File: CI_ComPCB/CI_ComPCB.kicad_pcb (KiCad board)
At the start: 2 copper layers, 83 x 85 mm, 37 parts, among them J1001 Conn_01x02_Male, J1002 Conn_01x02_Male, J1003 Conn_01x15_Female, J1004 Conn_01x15_Female, J1005 Conn_01x06_Female, J1006 Conn_01x06_Female, J1008 Conn_01x02_Male, J1009 RJ45_LED_Shielded, J1010 RJ45_LED_Shielded, J1011 Conn_01x01_Female, J1012 Conn_01x01_Female, J1013 Conn_02x04_Odd_Even, Q1001 IRF9540N, U1001 ESP32s, U1002 TPS54331

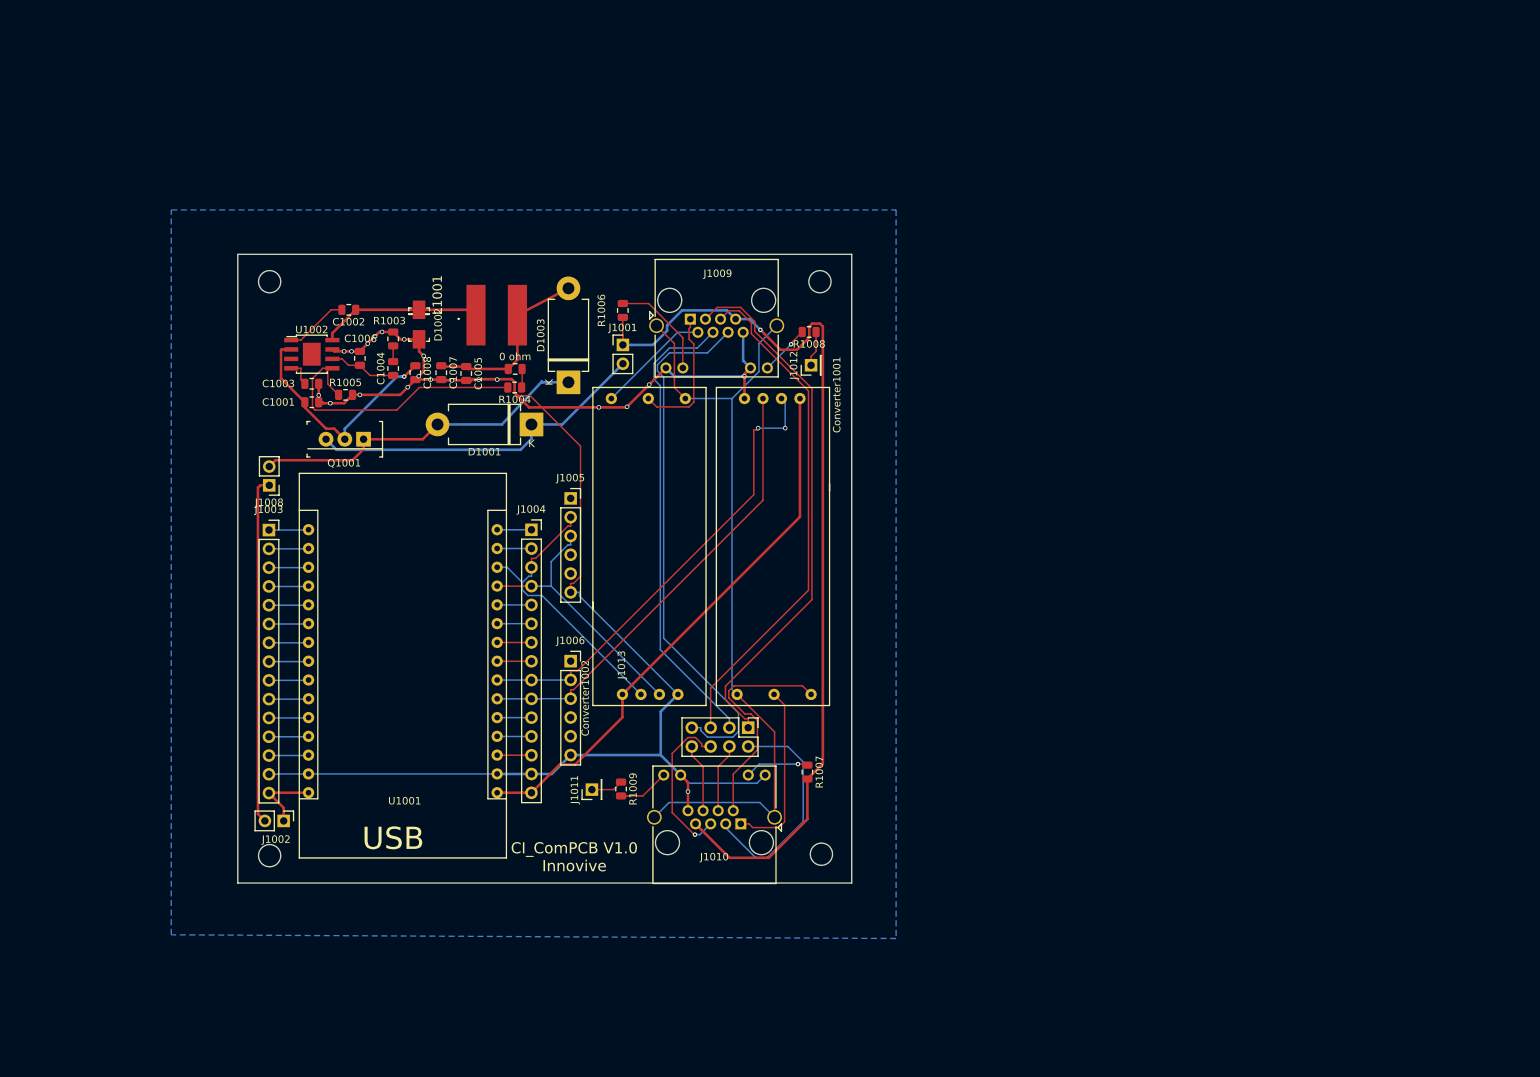
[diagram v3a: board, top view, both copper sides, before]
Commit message: V1.1 working progress
Implemented further documentation
New boost converter for the battery
power switches
Led indicator
removed unnecessary elements
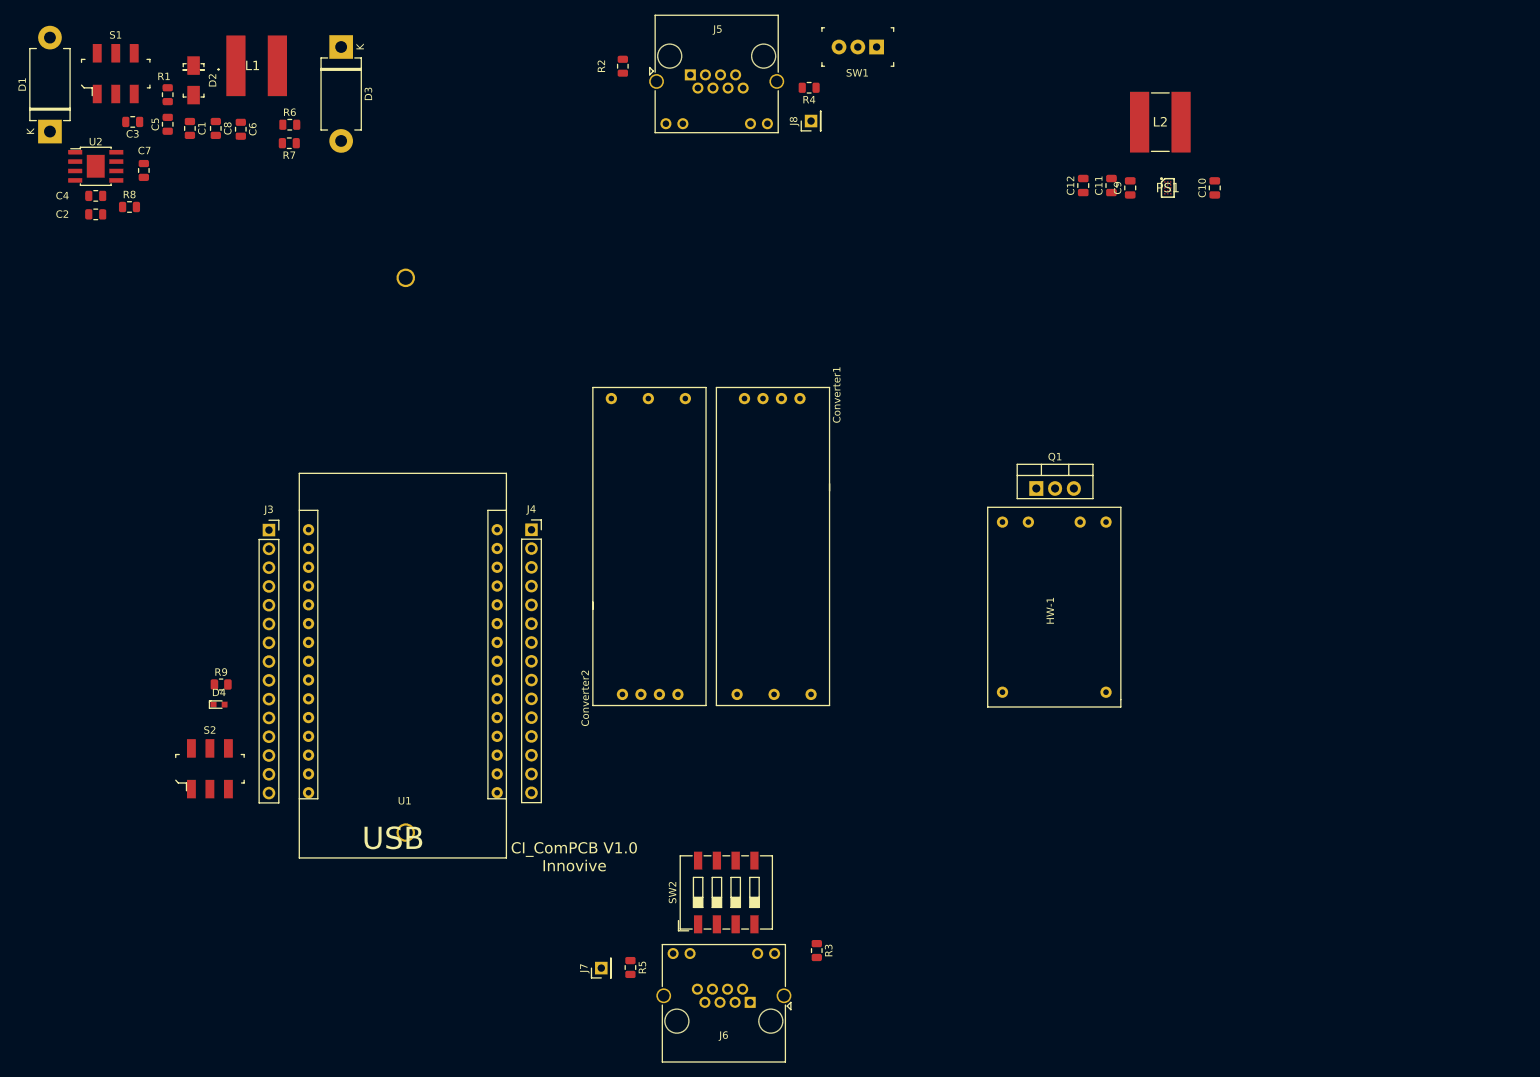
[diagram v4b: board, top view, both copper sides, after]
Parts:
- removed 0 ohm: 0, Resistor_SMD:R_0805_2012Metric
- removed C1002: 100nF, Capacitor_SMD:C_0805_2012Metric
- removed C1003: 8.2nF, Capacitor_SMD:C_0805_2012Metric
- removed C1004: 1nF, Capacitor_SMD:C_0805_2012Metric
- removed C1005, C1007: 47uF, Capacitor_SMD:C_0805_2012Metric
- removed C1006: 10pf, Capacitor_SMD:C_0805_2012Metric
- removed C1008: 10uF, Capacitor_SMD:C_0805_2012Metric
- removed D1001, D1003: 1N5400, Diode_THT:D_DO-201AD_P12.70mm_Horizontal
- removed D1002: B340A-13-F, digikey-footprints:DO-214AC
- removed J1001, J1002, J1008: Conn_01x02_Male, Connector_PinHeader_2.54mm:PinHeader_1x02_P2.54mm_Vertical
- removed J1003, J1004: Conn_01x15_Female, Connector_PinSocket_2.54mm:PinSocket_1x15_P2.54mm_Vertical
- removed J1005, J1006: Conn_01x06_Female, Connector_PinSocket_2.54mm:PinSocket_1x06_P2.54mm_Vertical
- removed J1009: RJ45_LED_Shielded, Connector_RJ:RJ45_Amphenol_RJHSE538X
- removed J1013: Conn_02x04_Odd_Even, Connector_PinHeader_2.54mm:PinHeader_2x04_P2.54mm_Vertical
- removed L1001: SRN8040-100M, SamacSys_Parts:SRN8040100M
- removed Q1001: IRF9540N, digikey-footprints:TO-220-3
- removed R1003: 49.9k, Resistor_SMD:R_0805_2012Metric
- removed R1004: 10.2k, Resistor_SMD:R_0805_2012Metric
- removed R1005: 1.91k, Resistor_SMD:R_0805_2012Metric
- removed R1006, R1008: 330, Resistor_SMD:R_0805_2012Metric
- removed U1001: ESP32s, CI_ComPCB:ESP32s
- removed U1002: TPS54331, Package_SO:TI_SO-PowerPAD-8
- added C1: 10uF, Capacitor_SMD:C_0805_2012Metric, F.Cu at (58.5, 61.0)
- added C10: C, Capacitor_SMD:C_0805_2012Metric, F.Cu at (197.1, 69.0)
- added C11: 22uf 3.71mohm, Capacitor_SMD:C_0805_2012Metric, F.Cu at (183.1, 68.7)
- added C12: 10uf 3mohm, Capacitor_SMD:C_0805_2012Metric, F.Cu at (179.3, 68.7)
- added C3: 100nF, Capacitor_SMD:C_0805_2012Metric, F.Cu at (50.8, 60.1)
- added C4: 8.2nF, Capacitor_SMD:C_0805_2012Metric, F.Cu at (45.8, 70.1)
- added C5: 1nF, Capacitor_SMD:C_0805_2012Metric, F.Cu at (55.5, 60.4)
- added C6: 47uF, Capacitor_SMD:C_0805_2012Metric, F.Cu at (65.4, 61.1)
- added C7: 10pf, Capacitor_SMD:C_0805_2012Metric, F.Cu at (52.3, 66.7)
- added C8: 47uF, Capacitor_SMD:C_0805_2012Metric, F.Cu at (62.0, 61.0)
- added C9: C, Capacitor_SMD:C_0805_2012Metric, F.Cu at (185.7, 69.0)
- added D1: 1N5400, Diode_THT:D_DO-201AD_P12.70mm_Horizontal, F.Cu at (39.6, 61.4)
- added D2: B340A-13-F, digikey-footprints:DO-214AC, F.Cu at (59.0, 54.5)
- added D3: 1N5400, Diode_THT:D_DO-201AD_P12.70mm_Horizontal, F.Cu at (79.0, 50.0)
- added D4: LTST-C190GKT, digikey-footprints:LED_0603, F.Cu at (62.5, 138.9)
- added HW-1: Charger-New_Library-RackComm-rescue-RackComm-rescue, CI_ComPCB:Charger, F.Cu at (184.4, 112.2)
- added Holder1: Battery-New_Library-RackComm-rescue, CI_ComPCB:Battery, B.Cu at (77.7, 79.2)
- added J3: Conn_01x15_Female, Connector_PinSocket_2.54mm:PinSocket_1x15_P2.54mm_Vertical, F.Cu at (69.2, 115.3)
- added J4: Conn_01x15_Female, Connector_PinSocket_2.54mm:PinSocket_1x15_P2.54mm_Vertical, F.Cu at (104.7, 115.2)
- added J5: RJ45_LED_Shielded, Connector_RJ:RJ45_Amphenol_RJHSE538X, F.Cu at (126.2, 53.7)
- added L1: SRN8040-100M, SamacSys_Parts:SRN8040100M, F.Cu at (67.5, 52.5)
- added L2: SRN8040-R50Y, SamacSys_Parts:SRN8040R50Y, F.Cu at (189.7, 60.1)
- added PS1: TPS63810YFFR, SamacSys_Parts:BGA15C40P3X5_134X226X62, F.Cu at (190.7, 69.0)
- added Q1: Transistor_FET_IRF9540N, Package_TO_SOT_THT:TO-220-3_Vertical, F.Cu at (172.9, 109.7)
- added R1: 49.9k, Resistor_SMD:R_0805_2012Metric, F.Cu at (55.5, 56.4)
- added R2: 680, Resistor_SMD:R_0805_2012Metric, F.Cu at (117.0, 52.6)
- added R4: 680, Resistor_SMD:R_0805_2012Metric, F.Cu at (142.2, 55.5)
- added R6: 0, Resistor_SMD:R_0805_2012Metric, F.Cu at (72.0, 60.5)
- added R7: 10.2k, Resistor_SMD:R_0805_2012Metric, F.Cu at (72.0, 63.0)
- added R8: 1.91k, Resistor_SMD:R_0805_2012Metric, F.Cu at (50.4, 71.6)
- added R9: 330, Resistor_SMD:R_0805_2012Metric, F.Cu at (62.7, 136.2)
- added S1: JS202011SCQN, digikey-footprints:Switch_Slide_JS202011SCQN, F.Cu at (48.5, 53.6)
- added S2: JS202011SCQN, digikey-footprints:Switch_Slide_JS202011SCQN, F.Cu at (61.2, 147.6)
- added SW1: SW_SPDT, digikey-footprints:Switch_Toggle_ATE1D-2M3-10-Z, F.Cu at (148.8, 50.0)
- added SW2: SW_DIP_x04, Button_Switch_SMD:SW_DIP_SPSTx04_Slide_9.78x12.34mm_W8.61mm_P2.54mm, F.Cu at (131.0, 164.3)
- added U1: ESP32s, CI_ComPCB:ESP32s, F.Cu at (73.3, 107.6)
- added U2: TPS54331, Package_SO:TI_SO-PowerPAD-8, F.Cu at (45.8, 66.1)
- R3: renamed from R1007; value 330 -> 680
- R5: renamed from R1009; value 330 -> 680
- moved C2 38.7 mm to (45.8, 72.6)
- moved J8 33.0 mm to (142.5, 60.0)
- moved J6 24.2 mm to (134.3, 179.1)
- moved J7 24.2 mm to (114.1, 174.5)
- moved R3 24.2 mm to (143.3, 172.1)
- moved R5 24.2 mm to (118.1, 174.4)
- renumbered C1001 to C2, Converter1001 to Converter1, Converter1002 to Converter2, J1010 to J6, J1011 to J7, J1012 to J8
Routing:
- net GND: track 250.4 -> 0.00 mm, vias 21 -> 0
- net EPower: track 124.6 -> 0.00 mm, vias 1 -> 0
- net Sheild: track 107.0 -> 0.00 mm
- net 3.3V: track 74.2 -> 0.00 mm
- net Net-(J1009-Pad6): track 72.8 -> 0.00 mm
- net Net-(J1009-Pad3): track 72.6 -> 0.00 mm
- net Net-(J1009-Pad5): track 68.7 -> 0.00 mm
- net TX2: track 63.2 -> 0.00 mm, vias 2 -> 0
- net Net-(J1009-Pad4): track 63.2 -> 0.00 mm
- net RX2: track 61.5 -> 0.00 mm
- net Vin: track 47.4 -> 0.00 mm
- net Net-(D1001-Pad1): track 46.7 -> 0.00 mm
- net Net-(D1001-Pad2): track 46.2 -> 0.00 mm
- net TX0: track 39.5 -> 0.00 mm
- net Net-(R1004-Pad2): track 39.2 -> 0.00 mm
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- removed copper zone on B.Cu, net GND
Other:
- board outline removed

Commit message: V1.1 in development
Implemented sheets
Added correct switches
Completed boost converter
REQUIRED before build:
PCB layout
Component matching with PCB maker
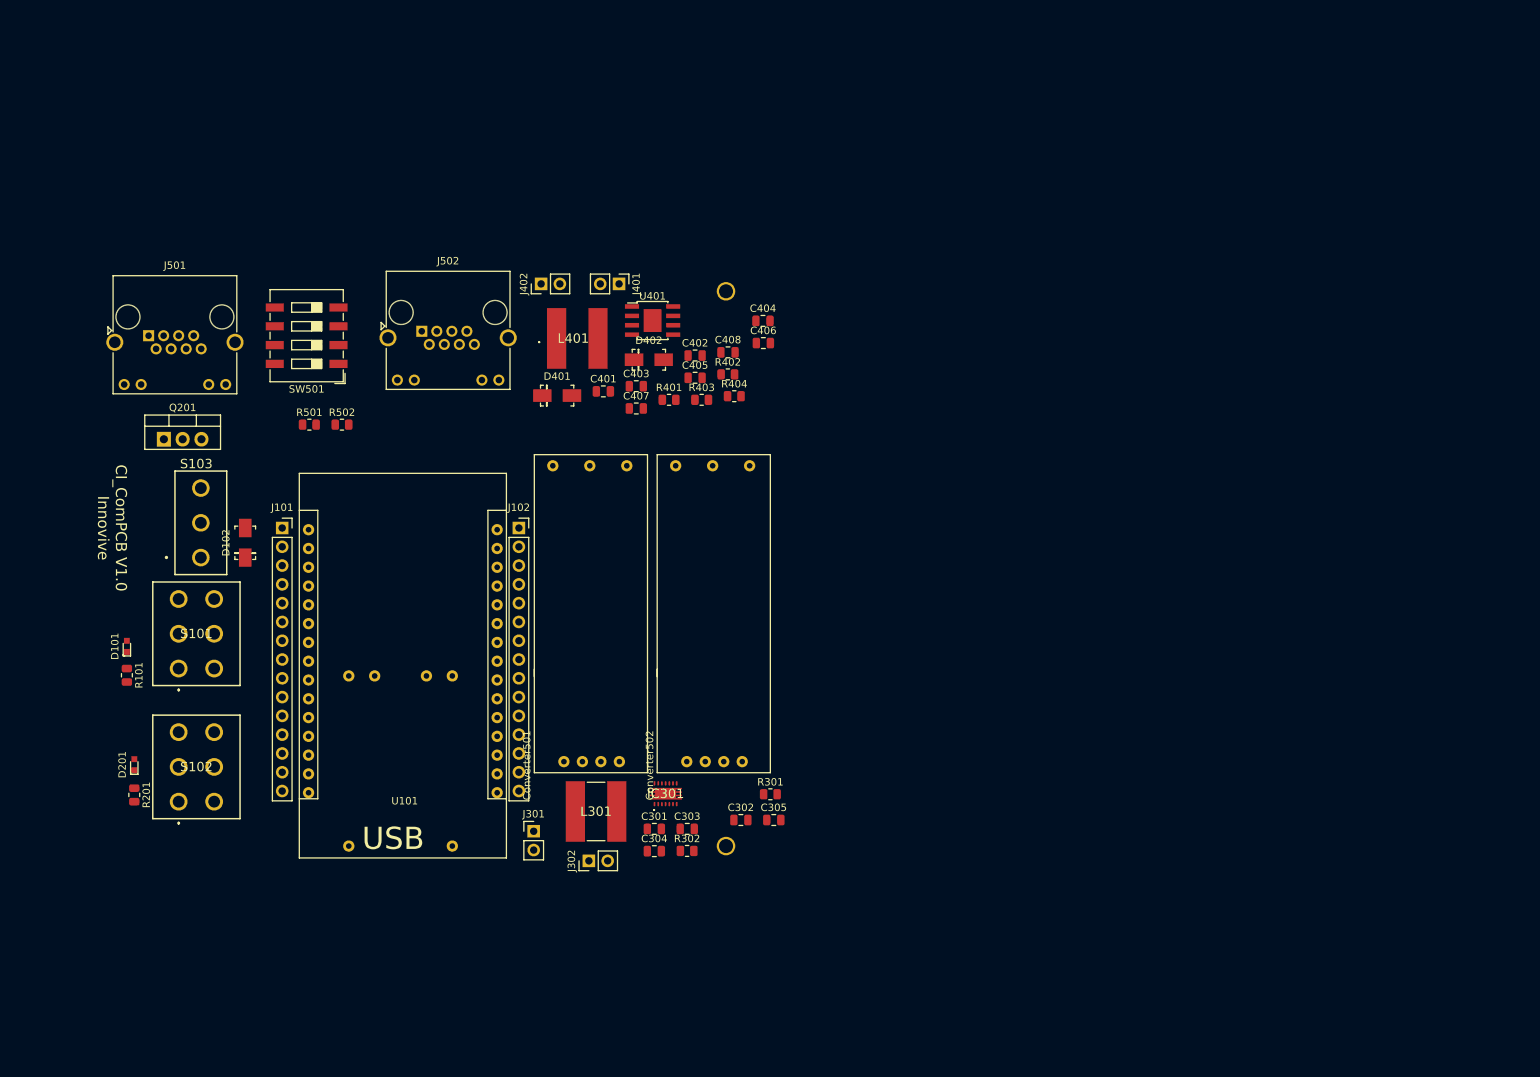
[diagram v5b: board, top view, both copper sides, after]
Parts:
- removed C1, C2: 10uF, Capacitor_SMD:C_0805_2012Metric
- removed C10, C9: C, Capacitor_SMD:C_0805_2012Metric
- removed C11: 22uf 3.71mohm, Capacitor_SMD:C_0805_2012Metric
- removed C12: 10uf 3mohm, Capacitor_SMD:C_0805_2012Metric
- removed C3: 100nF, Capacitor_SMD:C_0805_2012Metric
- removed C4: 8.2nF, Capacitor_SMD:C_0805_2012Metric
- removed C5: 1nF, Capacitor_SMD:C_0805_2012Metric
- removed C6, C8: 47uF, Capacitor_SMD:C_0805_2012Metric
- removed C7: 10pf, Capacitor_SMD:C_0805_2012Metric
- removed Converter1, Converter2: TxRx-RS485, CI_ComPCB:TXRX-AB
- removed D1, D3: 1N5400, Diode_THT:D_DO-201AD_P12.70mm_Horizontal
- removed D2: B340A-13-F, digikey-footprints:DO-214AC
- removed D4: LTST-C190GKT, digikey-footprints:LED_0603
- removed HW-1: Charger-New_Library-RackComm-rescue-RackComm-rescue, CI_ComPCB:Charger
- removed Holder1: Battery-New_Library-RackComm-rescue, CI_ComPCB:Battery
- removed J3, J4: Conn_01x15_Female, Connector_PinSocket_2.54mm:PinSocket_1x15_P2.54mm_Vertical
- removed J5, J6: RJ45_LED_Shielded, Connector_RJ:RJ45_Amphenol_RJHSE538X
- removed J7, J8: Conn_01x01_Female, Connector_PinHeader_2.54mm:PinHeader_1x01_P2.54mm_Vertical
- removed L1: SRN8040-100M, SamacSys_Parts:SRN8040100M
- removed L2: SRN8040-R50Y, SamacSys_Parts:SRN8040R50Y
- removed PS1: TPS63810YFFR, SamacSys_Parts:BGA15C40P3X5_134X226X62
- removed Q1: Transistor_FET_IRF9540N, Package_TO_SOT_THT:TO-220-3_Vertical
- removed R1: 49.9k, Resistor_SMD:R_0805_2012Metric
- removed R2, R3, R4, R5: 680, Resistor_SMD:R_0805_2012Metric
- removed R6: 0, Resistor_SMD:R_0805_2012Metric
- removed R7: 10.2k, Resistor_SMD:R_0805_2012Metric
- removed R8: 1.91k, Resistor_SMD:R_0805_2012Metric
- removed R9: 330, Resistor_SMD:R_0805_2012Metric
- removed S1, S2: JS202011SCQN, digikey-footprints:Switch_Slide_JS202011SCQN
- removed SW1: SW_SPDT, digikey-footprints:Switch_Toggle_ATE1D-2M3-10-Z
- removed SW2: SW_DIP_x04, Button_Switch_SMD:SW_DIP_SPSTx04_Slide_9.78x12.34mm_W8.61mm_P2.54mm
- removed U1: ESP32s, CI_ComPCB:ESP32s
- removed U2: TPS54331, Package_SO:TI_SO-PowerPAD-8
- added C301: 22uF, Capacitor_SMD:C_0805_2012Metric, F.Cu at (121.3, 155.7)
- added C302: 100nF, Capacitor_SMD:C_0805_2012Metric, F.Cu at (133.0, 154.5)
- added C303: 100nF, Capacitor_SMD:C_0805_2012Metric, F.Cu at (125.8, 155.7)
- added C304: 100nF, Capacitor_SMD:C_0805_2012Metric, F.Cu at (121.3, 158.7)
- added C305: 100nF, Capacitor_SMD:C_0805_2012Metric, F.Cu at (137.5, 154.5)
- added C401: 10uF, Capacitor_SMD:C_0805_2012Metric, F.Cu at (114.4, 96.5)
- added C402: 10uF, Capacitor_SMD:C_0805_2012Metric, F.Cu at (126.8, 91.7)
- added C403: 100nF, Capacitor_SMD:C_0805_2012Metric, F.Cu at (118.9, 95.8)
- added C404: 8.2nF, Capacitor_SMD:C_0805_2012Metric, F.Cu at (136.0, 87.0)
- added C405: 1nF, Capacitor_SMD:C_0805_2012Metric, F.Cu at (126.8, 94.7)
- added C406: 47uF, Capacitor_SMD:C_0805_2012Metric, F.Cu at (136.1, 90.0)
- added C407: 10pf, Capacitor_SMD:C_0805_2012Metric, F.Cu at (118.9, 98.8)
- added C408: 47uF, Capacitor_SMD:C_0805_2012Metric, F.Cu at (131.3, 91.2)
- added Converter501: TxRx-RS485, CI_ComPCB:TXRX-AB, F.Cu at (105.1, 148.1)
- added Converter502: TxRx-RS485, CI_ComPCB:TXRX-AB, F.Cu at (121.7, 148.1)
- added D101: LTST-C190GKT, digikey-footprints:LED_0603, F.Cu at (50.0, 131.0)
- added D102: B340A-13-F, digikey-footprints:DO-214AC, F.Cu at (66.0, 117.0)
- added D201: LTST-C190GKT, digikey-footprints:LED_0603, F.Cu at (51.0, 147.0)
- added D401: B340A-13-F, digikey-footprints:DO-214AC, F.Cu at (108.2, 97.1)
- added D402: B340A-13-F, digikey-footprints:DO-214AC, F.Cu at (120.6, 92.2)
- added HW-201: Charger-New_Library-RackComm-rescue-RackComm-rescue, CI_ComPCB:Charger, B.Cu at (78.0, 133.0)
- added Holder201: Battery-New_Library-RackComm-rescue, CI_ComPCB:Battery, B.Cu at (141.0, 160.0)
- added IC301: TPS63020DSJR, SamacSys_Parts:TPS63020DSJR, F.Cu at (122.8, 150.9)
- added J101: Conn_01x15_Female, Connector_PinSocket_2.54mm:PinSocket_1x15_P2.54mm_Vertical, F.Cu at (71.0, 115.0)
- added J102: Conn_01x15_Female, Connector_PinSocket_2.54mm:PinSocket_1x15_P2.54mm_Vertical, F.Cu at (103.0, 115.0)
- added J301: Connector_Conn_01x02_Male, Connector_PinHeader_2.54mm:PinHeader_1x02_P2.54mm_Vertical, F.Cu at (105.0, 156.0)
- added J302: Connector_Conn_01x02_Male, Connector_PinHeader_2.54mm:PinHeader_1x02_P2.54mm_Vertical, F.Cu at (112.5, 160.0)
- added J401: Connector_Conn_01x02_Male, Connector_PinHeader_2.54mm:PinHeader_1x02_P2.54mm_Vertical, F.Cu at (116.5, 82.0)
- added J402: Connector_Conn_01x02_Male, Connector_PinHeader_2.54mm:PinHeader_1x02_P2.54mm_Vertical, F.Cu at (106.0, 82.0)
- added J501: RJ45_LED_Shielded, Connector_RJ:RJ45_Amphenol_RJHSE538X, F.Cu at (52.9, 89.0)
- added J502: RJ45_LED_Shielded, Connector_RJ:RJ45_Amphenol_RJHSE538X, F.Cu at (89.9, 88.4)
- added L301: 1uH , 33mohm, SamacSys_Parts:SRN8040R50Y, F.Cu at (113.4, 153.3)
- added L401: SRN8040-100M, SamacSys_Parts:SRN8040100M, F.Cu at (110.9, 89.4)
- added Q201: Transistor_FET_IRF9540N, Package_TO_SOT_THT:TO-220-3_Vertical, F.Cu at (55.0, 103.0)
- added R101: 680, Resistor_SMD:R_0805_2012Metric, F.Cu at (50.0, 134.9)
- added R201: 330, Resistor_SMD:R_0805_2012Metric, F.Cu at (51.0, 151.1)
- added R301: 1.27M, Resistor_SMD:R_0805_2012Metric, F.Cu at (137.0, 151.0)
- added R302: 135k, Resistor_SMD:R_0805_2012Metric, F.Cu at (125.7, 158.7)
- added R401: 49.9k, Resistor_SMD:R_0805_2012Metric, F.Cu at (123.3, 97.7)
- added R402: 0, Resistor_SMD:R_0805_2012Metric, F.Cu at (131.2, 94.2)
- added R403: 10.2k, Resistor_SMD:R_0805_2012Metric, F.Cu at (127.7, 97.7)
- added R404: 1.91k, Resistor_SMD:R_0805_2012Metric, F.Cu at (132.1, 97.2)
- added R501: 680, Resistor_SMD:R_0805_2012Metric, F.Cu at (74.7, 101.0)
- added R502: 680, Resistor_SMD:R_0805_2012Metric, F.Cu at (79.1, 101.0)
- added S101: CS22BNW03, SamacSys_Parts:CS22BNW03, F.Cu at (57.0, 134.0)
- added S102: CS22BNW03, SamacSys_Parts:CS22BNW03, F.Cu at (57.0, 152.0)
- added S103: CS12ANW03, SamacSys_Parts:CS12ANW03, F.Cu at (60.0, 114.3)
- added SW501: SW_DIP_x04, Button_Switch_SMD:SW_DIP_SPSTx04_Slide_9.78x12.34mm_W8.61mm_P2.54mm, F.Cu at (74.3, 89.0)
- added U101: ESP32s, CI_ComPCB:ESP32s, F.Cu at (73.3, 107.6)
- added U401: TPS54331, Package_SO:TI_SO-PowerPAD-8, F.Cu at (121.1, 87.0)
